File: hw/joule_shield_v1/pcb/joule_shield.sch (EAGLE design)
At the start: 138 parts, among them J1 MF-CON-MICROUSB-RIGHT, J4 USB_AUSB_A_SMT_RA, J5 JST-ZH5JST_ZH_SMT_VERT, J6 INTEL_JOULE_J6, J7 INTEL_JOULE_J7, J8 DM3ATDM3AT, SW1 MF-SW-TACT-4.2MM, SW2 MF-SW-TACT-4.2MM, SW3 MF-SW-TACT-4.2MM, U1 BQ25892PWQFN-24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

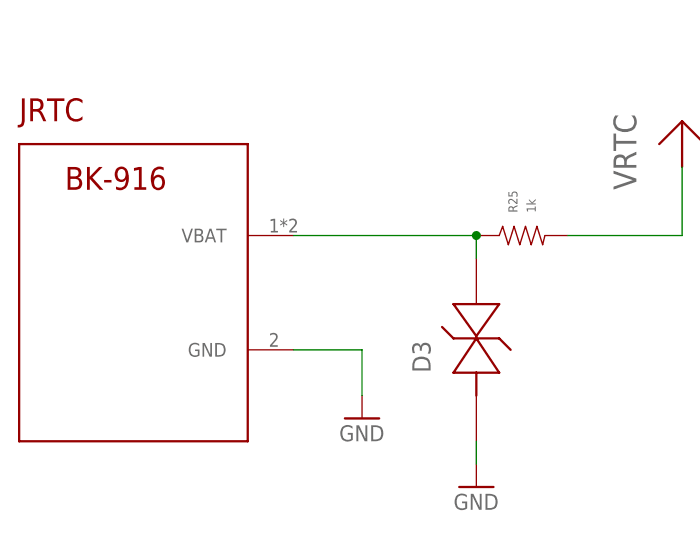
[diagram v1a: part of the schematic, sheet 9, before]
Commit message: joule shield: Switch to a smaller RTC battery and get everything on the board.
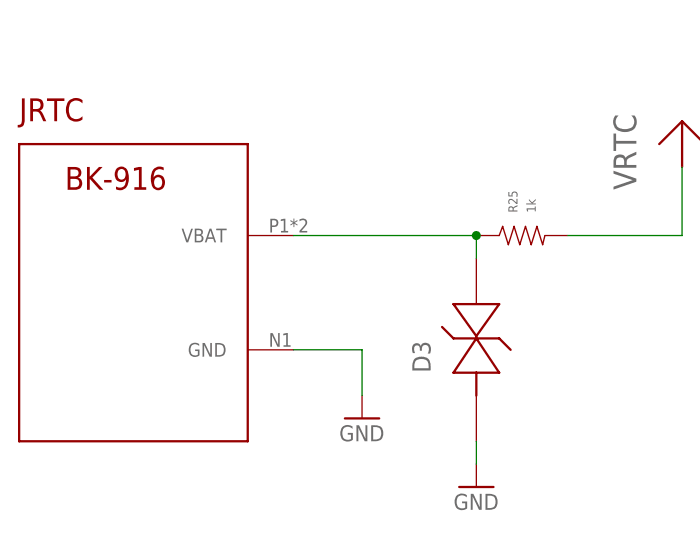
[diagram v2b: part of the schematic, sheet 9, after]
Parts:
- JRTC: value BK-916BK-916 -> BC-2009; device joule_shield:BK-916BK-916 -> joule_shield:BC-2009; DPN BK-916-CT-ND -> BC-2009-ND; MPN BK-916-TR -> BC-2009
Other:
- moved on the sheet: JRTC
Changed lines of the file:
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@@
 <part name="U$33" library="joule_shield" deviceset="V5P0V_USBB" device=""/>
 <part name="GND34" library="supply1" deviceset="GND" device=""/>
-<part name="JRTC" library="joule_shield" deviceset="BK-916" device="BK-916">
-<attribute name="DPN" value="BK-916-CT-ND"/>
+<part name="JRTC" library="joule_shield" deviceset="BC-2009" device="">
+<attribute name="DPN" value="BC-2009-ND"/>
 <attribute name="MF" value="MPD (Memory Protection Devices)"/>
-<attribute name="MPN" value="BK-916-TR"/>
+<attribute name="MPN" value="BC-2009"/>
 </part>
 <part name="GND35" library="supply1" deviceset="GND" device=""/>

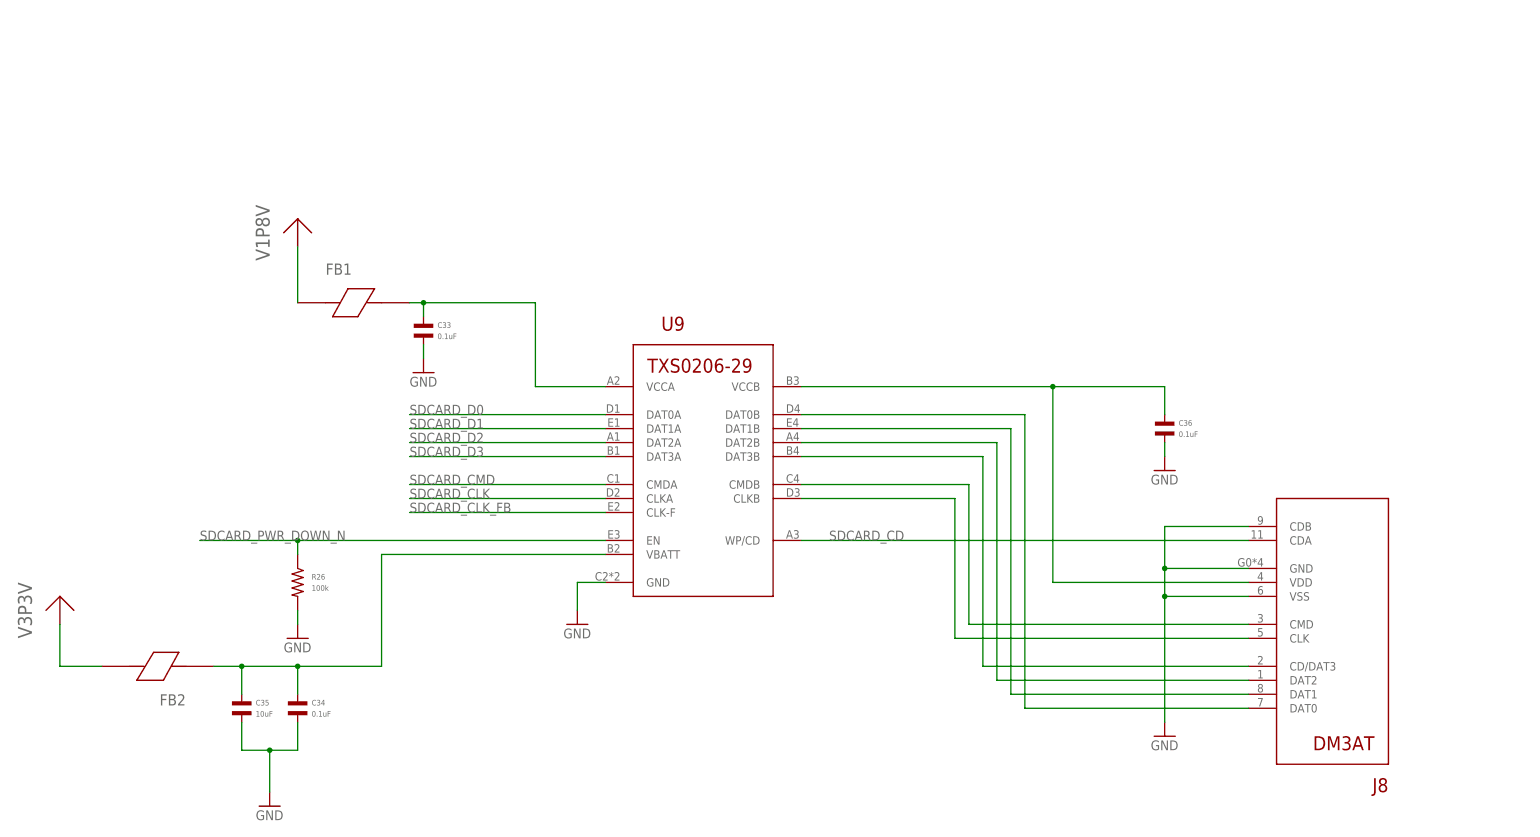
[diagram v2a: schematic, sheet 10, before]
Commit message: joule_shield: Swap SD level converter for one with a 0.5mm BGA pitch so that there is at least one macrofab process which can route it. Further work on draft placement.  Everything is kinda on the board now.
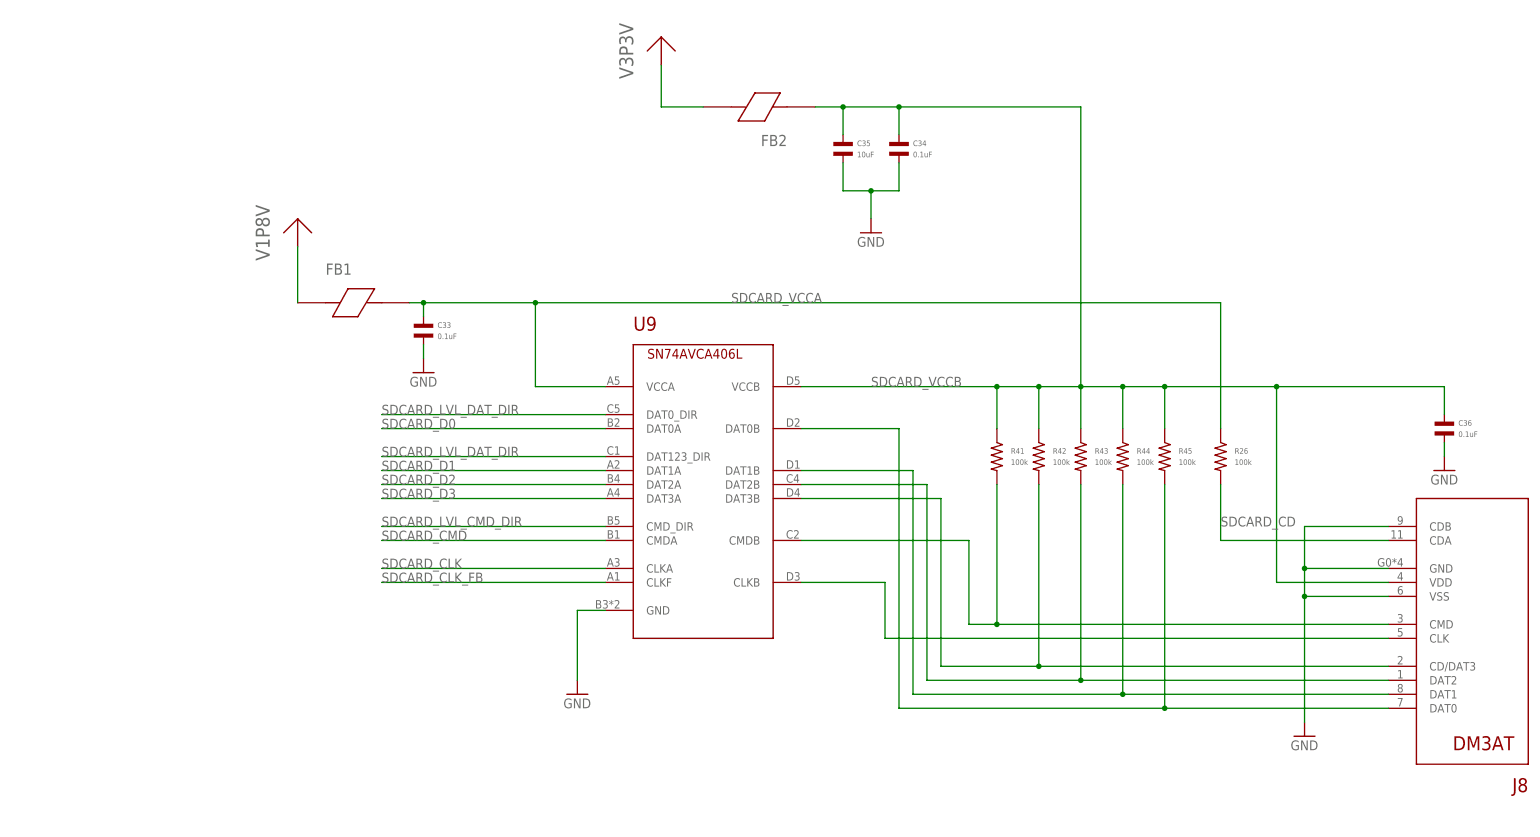
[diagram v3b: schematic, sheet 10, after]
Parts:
- added R41, R42, R43, R44, R45: 100k, mf_passives:RESISTOR_0603
- U9: value TXS0206-29 -> SN74AVCA406L; device joule_shield:TXS0206-29 -> joule_shield:SN74AVCA406L; DPN 296-25577-1-ND -> (none); MPN TXS0206-29YFPR -> (none)
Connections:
- removed net N$35: C36.P$1, J8.VDD, U9.VCCB
- removed net N$37: C34.P$1, C35.P$1, FB2.P$1, U9.VBATT
- removed net N$38: C33.P$1, FB1.P$2, U9.VCCA
- removed net N$40: J8.DAT0, U9.DAT0B
- new net N$69: J8.DAT0, R45.P$2, U9.DAT0B
- new net SDCARD_LVL_CMD_DIR: J6.SDCARD_LVL_CMD_DIR, U9.CMD_DIR
- new net SDCARD_LVL_DAT_DIR: J6.SDCARD_LVL_DAT_DIR, U9.DAT0_DIR, U9.DAT123_DIR
- new net SDCARD_VCCA: C33.P$1, FB1.P$2, R26.P$1, U9.VCCA
- new net SDCARD_VCCB: C34.P$1, C35.P$1, C36.P$1, FB2.P$1, J8.VDD, R41.P$1, R42.P$1, R43.P$1, R44.P$1, R45.P$1, U9.VCCB
- net GND: no longer R26.P$2
- net N$41: now also R44.P$2
- net N$42: now also R43.P$2
- net N$43: now also R42.P$2
- net N$44: now also R41.P$2
- net SDCARD_CD: now also R26.P$2; no longer U9.WP/CD
- net SDCARD_CLK_FB: now also U9.CLKF; no longer U9.CLK-F
- net SDCARD_PWR_DOWN_N: no longer R26.P$1, U9.EN
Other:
- moved on the sheet: C34, C35, C36, FB2, J8, R26, U9

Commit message: joule_shield: Connected up usb power switch enable and fault lines to GPIO pins.  Switched to smaller mosfets instead of MF house bipolars.
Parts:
- removed D11: MF-LED-0603-GREEN, mf_leds:LED_SINGLE-0603-GREEN
- removed U11, U12, U13, U14: MF-DSC-SOT233-MMBT3904, mf_discrete_semiconductor:NPN_BJTMMBT3904_SOT-23-3
- added Q1, Q2, Q3, Q4, Q5: NFETEMT3F, joule_shield:NFETEMT3F
- R36: value 1k -> 100k; MPN MF-RES-0603-1K -> MF-RES-0603-100K
- R40: value 470 -> 100k; MPN MF-RES-0603-470 -> MF-RES-0603-100K
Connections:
- removed net N$22: R19.P$2, U5.FAULT/
- removed net N$32: R22.P$2, U6.FAULT/
- removed net N$55: D11.ANODE, R40.P$2
- removed net N$62: D11.CATHODE, U14.COLLECTOR
- removed net N$63: R33.P$2, U11.BASE
- removed net N$64: R34.P$2, U12.BASE
- removed net N$65: R35.P$2, U13.BASE
- removed net N$66: R36.P$2, U14.BASE
- new net ISH_GPIO_4: J6.ISH_GPIO_4, Q5.G, R40.P$1
- new net ISH_GPIO_5: J6.ISH_GPIO_5, R19.P$2, U5.FAULT/
- new net ISH_GPIO_6: J6.ISH_GPIO_6, R22.P$2, U6.FAULT/
- net GND: now also Q1.S, Q2.S, Q3.S, Q4.S, Q5.S, R33.P$1, R34.P$1, R35.P$1, R36.P$2, R40.P$2; no longer U11.EMITTER, U12.EMITTER, U13.EMITTER, U14.EMITTER
- net ISH_GPIO_0: now also Q1.G, R33.P$2; no longer R33.P$1
- net ISH_GPIO_1: now also Q2.G, R34.P$2; no longer R34.P$1
- net ISH_GPIO_2: now also Q3.G, R35.P$2; no longer R35.P$1
- net ISH_GPIO_3: now also Q4.G
- net N$24: now also Q4.D
- net N$33: now also Q5.D
- net N$59: now also Q1.D; no longer U11.COLLECTOR
- net N$60: now also Q2.D; no longer U12.COLLECTOR
- net N$61: now also Q3.D; no longer U13.COLLECTOR
- net V5P0V: no longer R19.P$1, R22.P$1, R40.P$1
- net VDD1: now also R19.P$1, R22.P$1
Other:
- moved on the sheet: R33, R34, R35

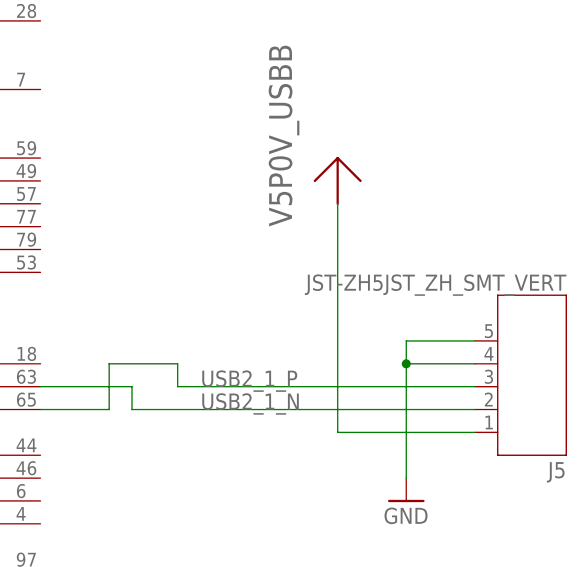
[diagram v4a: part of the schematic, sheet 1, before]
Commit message: joule shield: Made a pass at aligning all the parts.
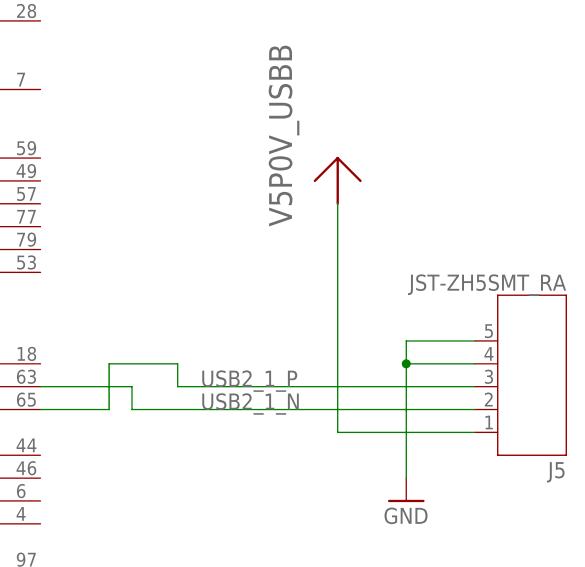
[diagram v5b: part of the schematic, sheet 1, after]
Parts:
- J5: value JST-ZH5JST_ZH_SMT_VERT -> JST-ZH5SMT_RA; device joule_shield:JST-ZH5JST_ZH_SMT_VERT -> joule_shield:JST-ZH5SMT_RA
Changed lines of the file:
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@@
 <part name="U$35" library="joule_shield" deviceset="V5P0V_USBB" device=""/>
 <part name="U$36" library="joule_shield" deviceset="V5P0V_USBA" device=""/>
-<part name="J5" library="joule_shield" deviceset="JST-ZH5" device="JST_ZH_SMT_VERT"/>
+<part name="J5" library="joule_shield" deviceset="JST-ZH5" device="SMT_RA" value="JST-ZH5SMT_RA"/>
 <part name="U$33" library="joule_shield" deviceset="V5P0V_USBB" device=""/>
 <part name="GND34" library="supply1" deviceset="GND" device=""/>
